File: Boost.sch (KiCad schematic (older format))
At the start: 23 parts, among them Q1 IRFZ44N, U1 UC3843_DIP8

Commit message: Modificado PCB y esquemático según clase del 31/06/19
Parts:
- COUT1: value 100u -> 1000u; footprint Capacitor_THT:CP_Radial_D8.0mm_P5.00mm -> Capacitor_THT:CP_Radial_D10.0mm_P5.00mm
- DOUT1: value 1N5819 -> 1N5822; symbol Diode:1N5819 -> Diode:1N5822
- RFB1: value 27k -> 22k
- RFB2: value 4k7 -> 3k3
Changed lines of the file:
@@
 $EndComp
 $Comp
-L Diode:1N5819 DOUT1
+L Diode:1N5822 DOUT1
 U 1 1 5CECB04F
 P 7250 2950
 F 0 "DOUT1" H 7250 2734 50  0000 C CNN
-F 1 "1N5819" H 7250 2825 50  0000 C CNN
+F 1 "1N5822" H 7250 2825 50  0000 C CNN
 F 2 "Diode_THT:D_DO-41_SOD81_P10.16mm_Horizontal" H 7250 2775 50  0001 C CNN
 F 3 "http://www.vishay.com/docs/88525/1n5817.pdf" H 7250 2950 50  0001 C CNN
@@
 P 8350 3750
 F 0 "RFB1" H 8420 3796 50  0000 L CNN
-F 1 "27k" H 8420 3705 50  0000 L CNN
+F 1 "22k" H 8420 3705 50  0000 L CNN
 F 2 "Resistor_THT:R_Axial_DIN0204_L3.6mm_D1.6mm_P7.62mm_Horizontal" V 8280 3750 50  0001 C CNN
 F 3 "~" H 8350 3750 50  0001 C CNN
@@
 P 8350 4400
 F 0 "RFB2" H 8420 4446 50  0000 L CNN
-F 1 "4k7" H 8420 4355 50  0000 L CNN
+F 1 "3k3" H 8420 4355 50  0000 L CNN
 F 2 "Resistor_THT:R_Axial_DIN0204_L3.6mm_D1.6mm_P7.62mm_Horizontal" V 8280 4400 50  0001 C CNN
 F 3 "~" H 8350 4400 50  0001 C CNN
@@
 P 7650 3250
 F 0 "COUT1" H 7768 3296 50  0000 L CNN
-F 1 "100u" H 7768 3205 50  0000 L CNN
-F 2 "Capacitor_THT:CP_Radial_D8.0mm_P5.00mm" H 7688 3100 50  0001 C CNN
+F 1 "1000u" H 7768 3205 50  0000 L CNN
+F 2 "Capacitor_THT:CP_Radial_D10.0mm_P5.00mm" H 7688 3100 50  0001 C CNN
 F 3 "~" H 7650 3250 50  0001 C CNN
 	1    7650 3250

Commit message: reemplazado IRFZ44N por IRFZ24N
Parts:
- Q1: value IRFZ44N -> IRFZ24N
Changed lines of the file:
@@
 P 6550 3300
 F 0 "Q1" H 6756 3346 50  0000 L CNN
-F 1 "IRFZ44N" H 6756 3255 50  0000 L CNN
+F 1 "IRFZ24N" H 6756 3255 50  0000 L CNN
 F 2 "Package_TO_SOT_THT:TO-220-3_Vertical" H 6800 3225 50  0001 L CIN
 F 3 "http://www.irf.com/product-info/datasheets/data/irlz44n.pdf" H 6550 3300 50  0001 L CNN

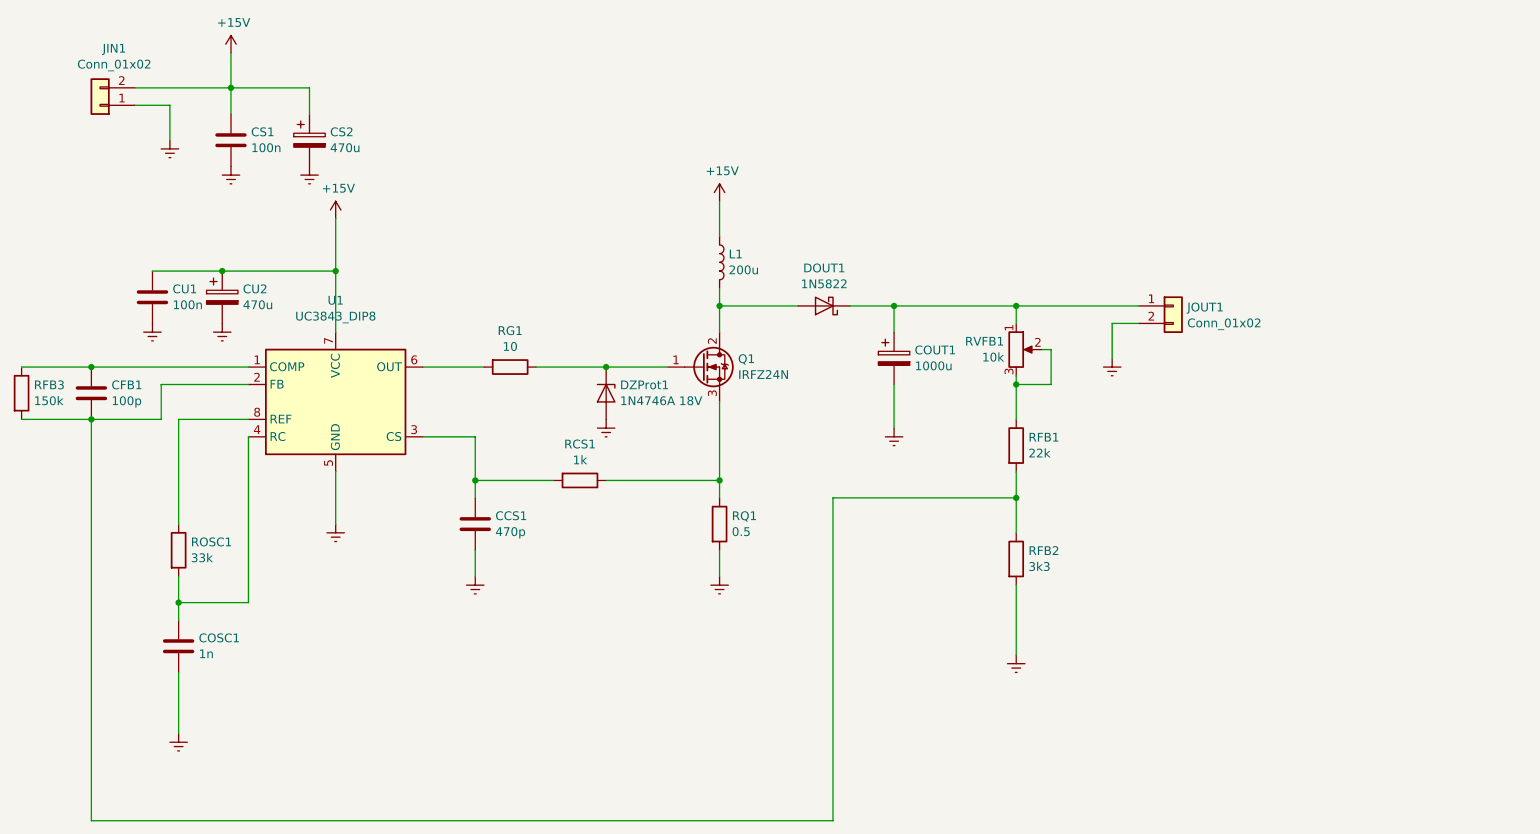
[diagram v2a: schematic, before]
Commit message: modificado esquematico y pcb, pero falta modificar pcb
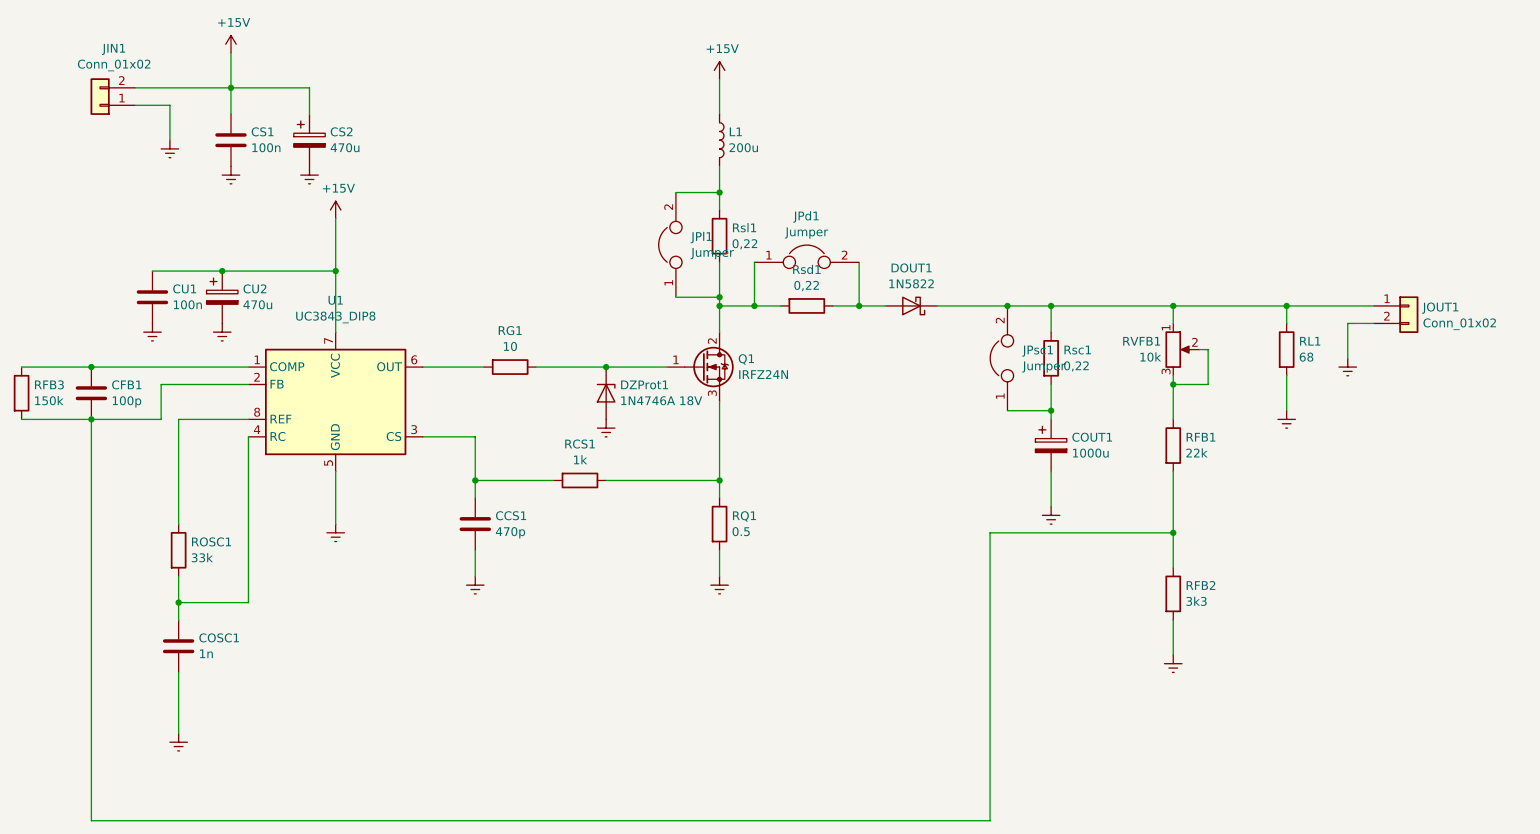
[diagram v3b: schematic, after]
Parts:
- added JPd1, JPl1, JPsc1: Jumper, Connector_PinHeader_2.54mm:PinHeader_1x02_P2.54mm_Vertical, symbol Device:Jumper
- added RL1: 68, Resistor_THT:R_Axial_Power_L50.0mm_W9.0mm_P60.96mm, symbol Device:R
- added Rsc1, Rsd1, Rsl1: 0,22, Resistor_THT:R_Axial_DIN0207_L6.3mm_D2.5mm_P10.16mm_Horizontal, symbol Device:R
- COSC1: footprint Capacitor_THT:C_Disc_D3.0mm_W2.0mm_P2.50mm -> Capacitor_THT:C_Disc_D3.4mm_W2.1mm_P2.50mm
- COUT1: footprint Capacitor_THT:CP_Radial_D10.0mm_P5.00mm -> Capacitor_THT:CP_Radial_D14.0mm_P5.00mm
- CU1: footprint Capacitor_THT:C_Disc_D3.0mm_W2.0mm_P2.50mm -> Capacitor_THT:C_Disc_D4.7mm_W2.5mm_P5.00mm
- CU2: footprint Capacitor_THT:CP_Radial_D4.0mm_P2.00mm -> Capacitor_THT:CP_Radial_D10.0mm_P5.00mm
- DOUT1: footprint Diode_THT:D_DO-41_SOD81_P10.16mm_Horizontal -> Diode_THT:D_DO-41_SOD81_P12.70mm_Horizontal
- RCS1, RFB1, RFB2, RFB3, RG1, ROSC1, RQ1: footprint Resistor_THT:R_Axial_DIN0204_L3.6mm_D1.6mm_P7.62mm_Horizontal -> Resistor_THT:R_Axial_DIN0207_L6.3mm_D2.5mm_P10.16mm_Horizontal
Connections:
- net Earth: now also RL1.2
- net at DOUT1.1 (K), JOUT1.1 (Pin_1), RVFB1.1: now also JPsc1.2, RL1.1, Rsc1.1; no longer COUT1.1
- new net: JPd1.1, JPl1.1, Q1.2 (D), Rsd1.2, Rsl1.2
- new net: DOUT1.2 (A), JPd1.2, Rsd1.1
- new net: COUT1.1, JPsc1.1, Rsc1.2
- new net: JPl1.2, L1.2, Rsl1.1
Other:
- moved on the sheet: COUT1, DOUT1, JOUT1, L1, RFB1, RFB2, RVFB1

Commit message: acomodado pcb a 10x10 con bobina casi de la medida y disipador del FET, resta corroborar medidas de los mismos
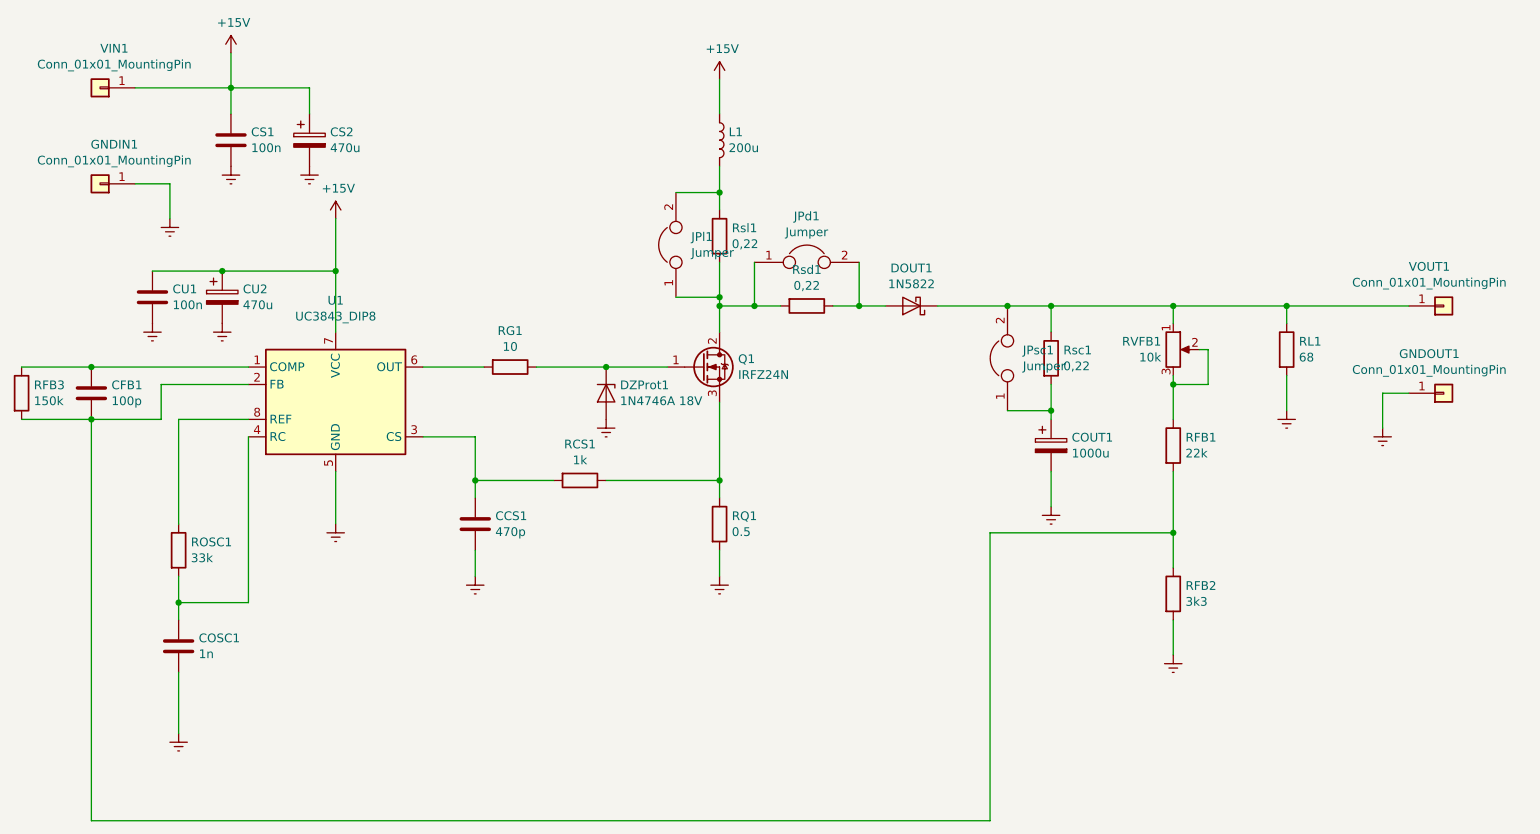
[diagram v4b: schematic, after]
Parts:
- removed JIN1, JOUT1: Conn_01x02, Connector:Banana_Jack_2Pin, symbol Connector_Generic:Conn_01x02
- added GNDIN1, GNDOUT1, VIN1, VOUT1: Conn_01x01_MountingPin, Connector:Banana_Jack_1Pin, symbol Connector_Generic:Conn_01x01
- CS1: footprint Capacitor_THT:C_Disc_D3.0mm_W2.0mm_P2.50mm -> Capacitor_THT:C_Disc_D4.7mm_W2.5mm_P5.00mm
- CS2: footprint Capacitor_THT:CP_Radial_D4.0mm_P2.00mm -> Capacitor_THT:CP_Radial_D10.0mm_P5.00mm
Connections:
- net +15V: now also VIN1.1 (Pin_1)
- net Earth: now also GNDIN1.1 (Pin_1), GNDOUT1.1 (Pin_1)
- net at DOUT1.1 (K), JPsc1.2, RL1.1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: now also VOUT1.1 (Pin_1)
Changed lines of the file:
@@
 F 0 "CS2" H 4418 2046 50  0000 L CNN
 F 1 "470u" H 4418 1955 50  0000 L CNN
-F 2 "Capacitor_THT:CP_Radial_D4.0mm_P2.00mm" H 4338 1850 50  0001 C CNN
+F 2 "Capacitor_THT:CP_Radial_D10.0mm_P5.00mm" H 4338 1850 50  0001 C CNN
 F 3 "~" H 4300 2000 50  0001 C CNN
 	1    4300 2000
@@
 F 0 "CS1" H 3965 2046 50  0000 L CNN
 F 1 "100n" H 3965 1955 50  0000 L CNN
-F 2 "Capacitor_THT:C_Disc_D3.0mm_W2.0mm_P2.50mm" H 3888 1850 50  0001 C CNN
+F 2 "Capacitor_THT:C_Disc_D4.7mm_W2.5mm_P5.00mm" H 3888 1850 50  0001 C CNN
 F 3 "~" H 3850 2000 50  0001 C CNN
 	1    3850 2000
@@
 	3050 3600 3450 3600
 $Comp
-L Connector_Generic:Conn_01x02 JOUT1
-U 1 1 5CEED7D8
-P 10600 2950
-F 0 "JOUT1" H 10680 2942 50  0000 L CNN
-F 1 "Conn_01x02" H 10680 2851 50  0000 L CNN
-F 2 "Connector:Banana_Jack_2Pin" H 10600 2950 50  0001 C CNN
-F 3 "~" H 10600 2950 50  0001 C CNN
-	1    10600 2950
-	1    0    0    -1
-$EndComp
-$Comp
-L Connector_Generic:Conn_01x02 JIN1
-U 1 1 5CEEE4AB
-P 3100 1800
-F 0 "JIN1" H 3018 1475 50  0000 C CNN
-F 1 "Conn_01x02" H 3018 1566 50  0000 C CNN
-F 2 "Connector:Banana_Jack_2Pin" H 3100 1800 50  0001 C CNN
-F 3 "~" H 3100 1800 50  0001 C CNN
-	1    3100 1800
-	-1   0    0    1
-$EndComp
-$Comp
 L power:Earth #PWR0115
 U 1 1 5CEEFC93
-P 10250 3250
-F 0 "#PWR0115" H 10250 3000 50  0001 C CNN
-F 1 "Earth" H 10250 3100 50  0001 C CNN
-F 2 "" H 10250 3250 50  0001 C CNN
-F 3 "~" H 10250 3250 50  0001 C CNN
-	1    10250 3250
-	1    0    0    -1
-$EndComp
-Wire Wire Line
-	10400 3050 10250 3050
-Wire Wire Line
-	10250 3050 10250 3250
+P 10450 3650
+F 0 "#PWR0115" H 10450 3400 50  0001 C CNN
+F 1 "Earth" H 10450 3500 50  0001 C CNN
+F 2 "" H 10450 3650 50  0001 C CNN
+F 3 "~" H 10450 3650 50  0001 C CNN
+	1    10450 3650
+	1    0    0    -1
+$EndComp
+Wire Wire Line
+	10600 3450 10450 3450
+Wire Wire Line
+	10450 3450 10450 3650
 $Comp
 L power:Earth #PWR0116
 U 1 1 5CEF216B
-P 3500 2000
-F 0 "#PWR0116" H 3500 1750 50  0001 C CNN
-F 1 "Earth" H 3500 1850 50  0001 C CNN
-F 2 "" H 3500 2000 50  0001 C CNN
-F 3 "~" H 3500 2000 50  0001 C CNN
-	1    3500 2000
-	1    0    0    -1
-$EndComp
-Wire Wire Line
-	3300 1800 3500 1800
-Wire Wire Line
-	3500 1800 3500 2000
-Wire Wire Line
-	3300 1700 3850 1700
+P 3500 2450
+F 0 "#PWR0116" H 3500 2200 50  0001 C CNN
+F 1 "Earth" H 3500 2300 50  0001 C CNN
+F 2 "" H 3500 2450 50  0001 C CNN
+F 3 "~" H 3500 2450 50  0001 C CNN
+	1    3500 2450
+	1    0    0    -1
+$EndComp
+Wire Wire Line
+	3300 2250 3500 2250
+Wire Wire Line
+	3500 2250 3500 2450
 $Comp
 L Device:CP COUT1
@@
 Wire Wire Line
 	9900 3050 9900 2950
-Connection ~ 9900 2950
-Wire Wire Line
-	9900 2950 10400 2950
 Wire Wire Line
 	9250 3900 9250 4250
@@
 Wire Wire Line
 	3050 5900 8200 5900
+$Comp
+L Connector_Generic:Conn_01x01 GNDIN1
+U 1 1 5D06B046
+P 3100 2250
+F 0 "GNDIN1" H 3018 2025 50  0000 C CNN
+F 1 "Conn_01x01_MountingPin" H 3018 2116 50  0000 C CNN
+F 2 "Connector:Banana_Jack_1Pin" H 3100 2250 50  0001 C CNN
+F 3 "~" H 3100 2250 50  0001 C CNN
+	1    3100 2250
+	-1   0    0    1
+$EndComp
+$Comp
+L Connector_Generic:Conn_01x01 VIN1
+U 1 1 5D05FFB3
+P 3100 1700
+F 0 "VIN1" H 3018 1475 50  0000 C CNN
+F 1 "Conn_01x01_MountingPin" H 3018 1566 50  0000 C CNN
+F 2 "Connector:Banana_Jack_1Pin" H 3100 1700 50  0001 C CNN
+F 3 "~" H 3100 1700 50  0001 C CNN
+	1    3100 1700
+	-1   0    0    1
+$EndComp
+$Comp
+L Connector_Generic:Conn_01x01 GNDOUT1
+U 1 1 5D0729F8
+P 10800 3450
+F 0 "GNDOUT1" H 10718 3225 50  0000 C CNN
+F 1 "Conn_01x01_MountingPin" H 10718 3316 50  0000 C CNN
+F 2 "Connector:Banana_Jack_1Pin" H 10800 3450 50  0001 C CNN
+F 3 "~" H 10800 3450 50  0001 C CNN
+	1    10800 3450
+	1    0    0    1
+$EndComp
+$Comp
+L Connector_Generic:Conn_01x01 VOUT1
+U 1 1 5D0729FE
+P 10800 2950
+F 0 "VOUT1" H 10718 2725 50  0000 C CNN
+F 1 "Conn_01x01_MountingPin" H 10718 2816 50  0000 C CNN
+F 2 "Connector:Banana_Jack_1Pin" H 10800 2950 50  0001 C CNN
+F 3 "~" H 10800 2950 50  0001 C CNN
+	1    10800 2950
+	1    0    0    1
+$EndComp
+Wire Wire Line
+	9900 2950 10600 2950
+Connection ~ 9900 2950
+Wire Wire Line
+	3300 1700 3850 1700
 $EndSCHEMATC

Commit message: Disipador + Bobina.
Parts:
- L1: footprint Inductor_THT:L_Axial_L9.5mm_D4.0mm_P15.24mm_Horizontal_Fastron_SMCC -> Inductor_THT:Inductor_26mm_x_8mm
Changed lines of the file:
@@
-	1    0    0    -1
-$EndComp
-$Comp
-L Device:L L1
-U 1 1 5CED603A
-P 6650 2000
-F 0 "L1" H 6702 2046 50  0000 L CNN
-F 1 "200u" H 6702 1955 50  0000 L CNN
-F 2 "Inductor_THT:L_Axial_L9.5mm_D4.0mm_P15.24mm_Horizontal_Fastron_SMCC" H 6650 2000 50  0001 C CNN
-F 3 "~" H 6650 2000 50  0001 C CNN
-	1    6650 2000
 	1    0    0    -1
 $EndComp
@@
 Wire Wire Line
 	3300 1700 3850 1700
+$Comp
+L Device:L L1
+U 1 1 5CED603A
+P 6650 2000
+F 0 "L1" H 6702 2046 50  0000 L CNN
+F 1 "200u" H 6702 1955 50  0000 L CNN
+F 2 "Inductor_THT:Inductor_26mm_x_8mm" H 6650 2000 50  0001 C CNN
+F 3 "~" H 6650 2000 50  0001 C CNN
+	1    6650 2000
+	1    0    0    -1
+$EndComp
 $EndSCHEMATC
